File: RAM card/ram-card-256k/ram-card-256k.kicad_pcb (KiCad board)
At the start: 2 copper layers, 88.9 x 53.3 mm, 12 parts, among them J1 RAM card connector, U1 HC138, U2 KM681000BLG, U3 KM681000BLG

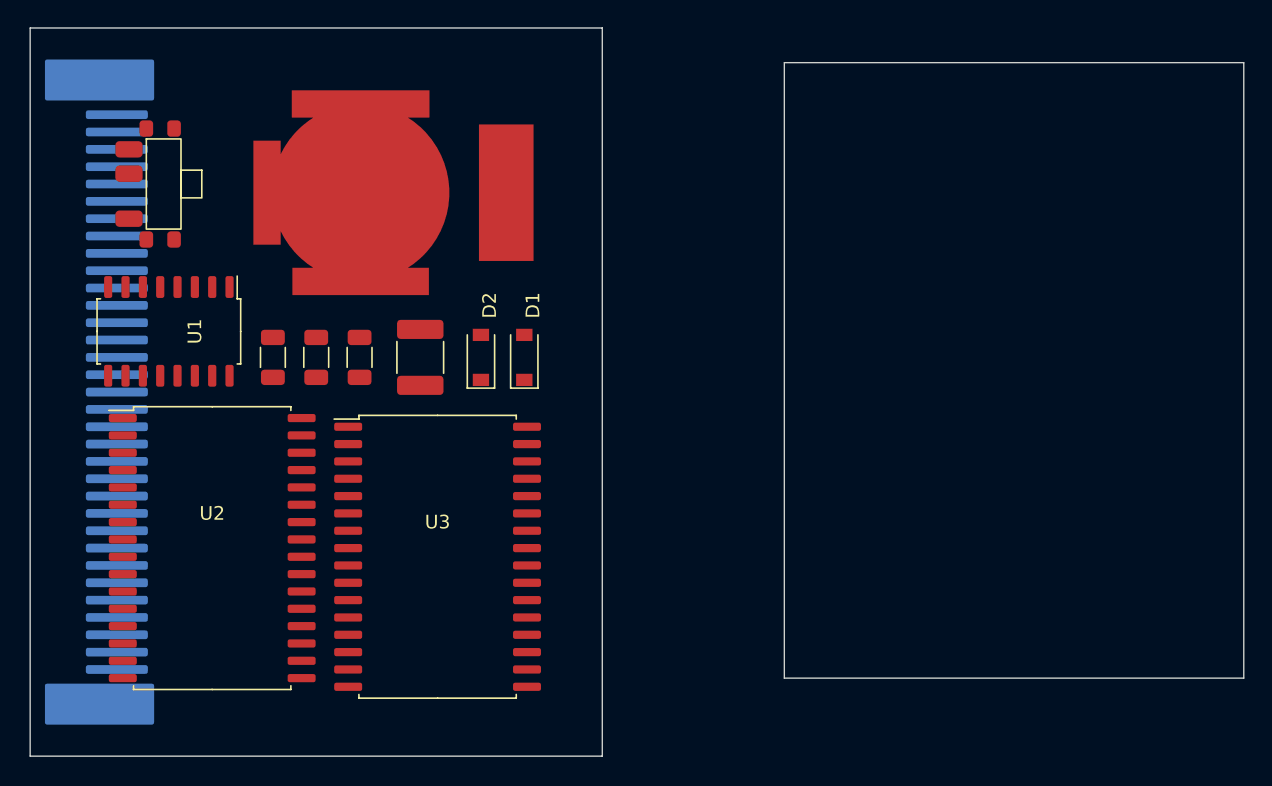
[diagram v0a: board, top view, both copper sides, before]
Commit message: Component layout
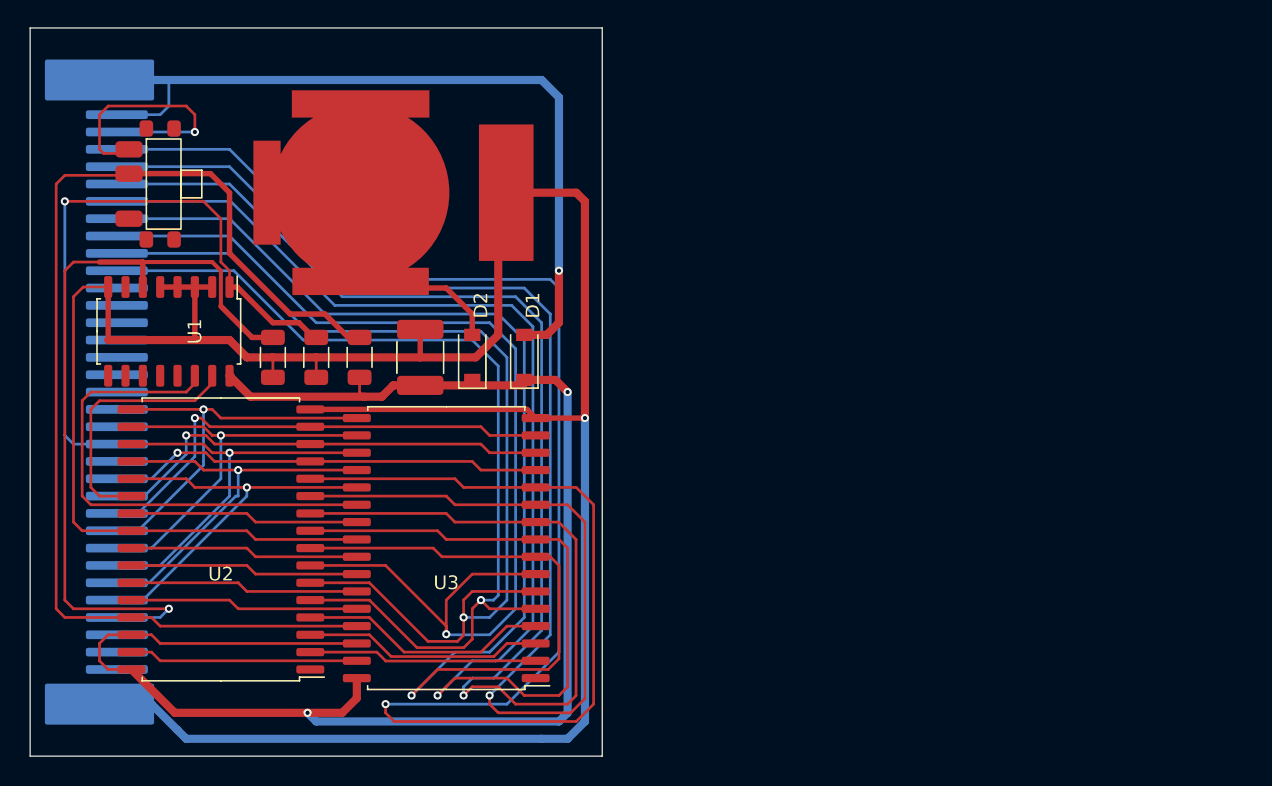
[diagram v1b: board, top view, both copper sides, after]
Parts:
- moved U2 0.90 mm to (128.3, 75.6), turned to 180 degrees
- moved U3 0.90 mm to (144.8, 76.2), turned to 180 degrees
- moved D2 0.63 mm to (146.7, 62.2)
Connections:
- S1 pad 1: R/W -> Net-(J1-Pad3)
- S1 pad 2: Net-(J1-Pad3) -> R/W
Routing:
- net GND: track 0.00 -> 193.9 mm, vias 0 -> 1
- net /A0: track 0.00 -> 130.4 mm, vias 0 -> 1
- net VCC: track 0.00 -> 113.1 mm, vias 0 -> 2
- net /A1: track 0.00 -> 108.2 mm, vias 0 -> 1
- net /A2: track 0.00 -> 106.9 mm, vias 0 -> 1
- net /A3: track 0.00 -> 105.7 mm, vias 0 -> 1
- net /A4: track 0.00 -> 102.0 mm, vias 0 -> 1
- net R/W: track 0.00 -> 83.0 mm
- net /A5: track 0.00 -> 79.8 mm, vias 0 -> 1
- net /A6: track 0.00 -> 74.5 mm, vias 0 -> 1
- net /A7: track 0.00 -> 70.0 mm, vias 0 -> 1
- net Net-(D1-Pad2): track 0.00 -> 59.6 mm, vias 0 -> 1
- net Net-(J1-Pad31): track 0.00 -> 57.2 mm, vias 0 -> 1
- net Net-(J1-Pad21): track 0.00 -> 45.5 mm, vias 0 -> 1
- net Net-(U1-Pad14): track 0.00 -> 36.7 mm
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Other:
- board size 88.9 x 53.3 mm -> 41.9 x 53.3 mm

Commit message: Layout
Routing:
- net (no net): track 0.00 -> 108.2 mm
- net /A10: track 16.8 -> 77.5 mm, vias 0 -> 1
- net /A8: track 16.8 -> 74.5 mm, vias 0 -> 1
- net /A9: track 16.8 -> 73.6 mm, vias 0 -> 1
- net /A11: track 16.8 -> 71.3 mm
- net /A0: track 130.4 -> 128.7 mm

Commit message: Layout
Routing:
- net /A0: track 128.7 -> 16.8 mm, vias 1 -> 0
- net /A1: track 108.2 -> 16.8 mm, vias 1 -> 0
- net /A2: track 106.9 -> 16.8 mm, vias 1 -> 0
- net /A3: track 105.7 -> 16.8 mm, vias 1 -> 0
- net /A4: track 102.0 -> 16.8 mm, vias 1 -> 0
- net /A5: track 79.8 -> 0.00 mm, vias 1 -> 0
- net /A6: track 74.5 -> 0.00 mm, vias 1 -> 0
- net /A7: track 70.0 -> 0.00 mm, vias 1 -> 0
- net /A10: track 77.5 -> 16.8 mm, vias 1 -> 0
- net /A8: track 74.5 -> 16.8 mm, vias 1 -> 0
- net /A9: track 73.6 -> 16.8 mm, vias 1 -> 0
- net /A11: track 71.3 -> 16.8 mm
- net Net-(J1-Pad31): track 57.2 -> 15.1 mm, vias 1 -> 0
- net /D2: track 35.7 -> 16.8 mm, vias 1 -> 0
- net /A12: track 18.4 -> 0.00 mm
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
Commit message: Layout
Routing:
- net (no net): track 108.2 -> 0.00 mm
- net Net-(J1-Pad31): track 15.1 -> 55.9 mm, vias 0 -> 1
- net /A6: track 0.00 -> 16.8 mm
- net /A14: track 0.00 -> 16.8 mm
- net /A12: track 0.00 -> 16.8 mm
- net /A5: track 0.00 -> 16.8 mm
- net /A7: track 0.00 -> 16.8 mm
